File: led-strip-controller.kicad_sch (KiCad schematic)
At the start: 20 parts, among them J1 5.5/2.1, J2 PROG, J3 LED strip, Q1 BD681, Q2 BD681, Q3 BD681, SW1 PRG, SW2 RST, U1 12V->3V3, U2 ESP-201

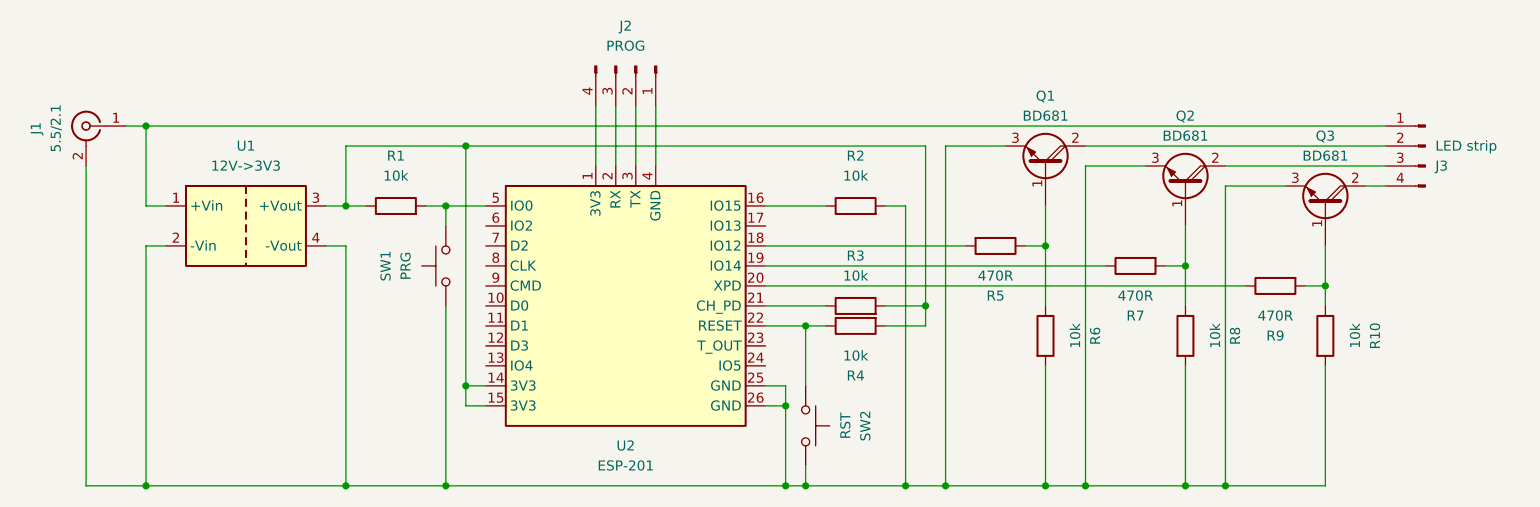
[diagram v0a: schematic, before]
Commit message: PINs 12, 13 and 14 used instead of 12, 14 and 16 (the original configuration caused flashing while device restarting)
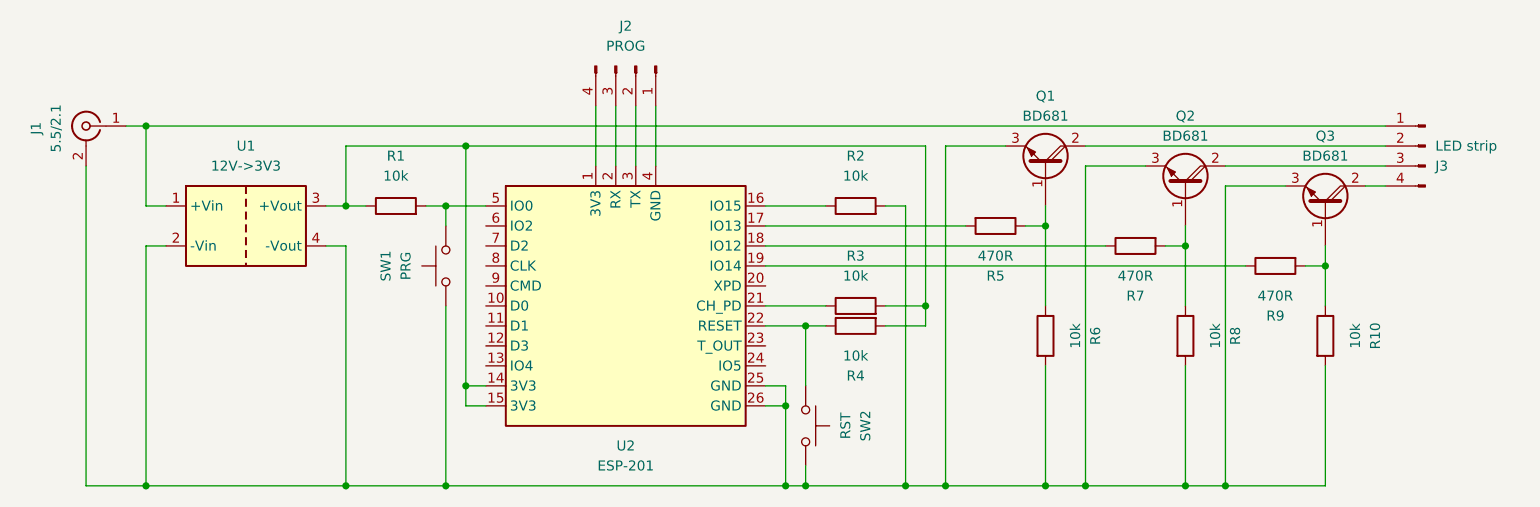
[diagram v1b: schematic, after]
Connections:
- net at U2.17 (IO13): now also R5.2
- net at U2.18 (IO12): now also R7.1; no longer R5.2
- net at U2.19 (IO14): now also R9.1; no longer R7.1
- net at U2.20 (XPD): no longer R9.1
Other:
- moved on the sheet: R5, R7, R9
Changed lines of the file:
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@@
 		(title "LED strip controller")
 		(date "2024-09-21")
-		(rev "1.0")
+		(rev "1.1")
 		(company "Eli Nucknack")
 	)
@@
 	)
 	(junction
-		(at 190.5 88.9)
-		(diameter 0)
-		(color 0 0 0 0)
-	)
-	(junction
 		(at 114.3 119.38)
 		(diameter 0)
@@
 	)
 	(junction
-		(at 208.28 91.44)
-		(diameter 0)
-		(color 0 0 0 0)
-	)
-	(junction
 		(at 175.26 96.52)
 		(diameter 0)
@@
 	)
 	(junction
+		(at 208.28 88.9)
+		(diameter 0)
+		(color 0 0 0 0)
+	)
+	(junction
 		(at 116.84 76.2)
 		(diameter 0)
@@
 	)
 	(junction
-		(at 226.06 93.98)
+		(at 226.06 91.44)
 		(diameter 0)
 		(color 0 0 0 0)
@@
 	)
 	(junction
+		(at 190.5 86.36)
+		(diameter 0)
+		(color 0 0 0 0)
+	)
+	(junction
 		(at 190.5 119.38)
 		(diameter 0)
@@
 	(wire
 		(pts
-			(xy 208.28 91.44) (xy 208.28 96.52)
-		)
-		(stroke
-			(width 0)
-			(type default)
-		)
-	)
-	(wire
-		(pts
 			(xy 172.72 119.38) (xy 177.8 119.38)
 		)
@@
 	(wire
 		(pts
-			(xy 154.94 88.9) (xy 180.34 88.9)
-		)
-		(stroke
-			(width 0)
-			(type default)
-		)
-	)
-	(wire
-		(pts
 			(xy 116.84 76.2) (xy 116.84 106.68)
 		)
@@
 	(wire
 		(pts
-			(xy 190.5 83.82) (xy 190.5 88.9)
+			(xy 190.5 83.82) (xy 190.5 86.36)
 		)
 		(stroke
@@
 	(wire
 		(pts
-			(xy 226.06 93.98) (xy 226.06 96.52)
+			(xy 226.06 91.44) (xy 226.06 96.52)
 		)
 		(stroke
@@
 	(wire
 		(pts
-			(xy 187.96 88.9) (xy 190.5 88.9)
+			(xy 187.96 86.36) (xy 190.5 86.36)
+		)
+		(stroke
+			(width 0)
+			(type default)
+		)
+	)
+	(wire
+		(pts
+			(xy 154.94 91.44) (xy 215.9 91.44)
 		)
 		(stroke
@@
 	(wire
 		(pts
-			(xy 223.52 93.98) (xy 226.06 93.98)
+			(xy 223.52 91.44) (xy 226.06 91.44)
 		)
 		(stroke
@@
 	(wire
 		(pts
-			(xy 154.94 93.98) (xy 215.9 93.98)
-		)
-		(stroke
-			(width 0)
-			(type default)
-		)
-	)
-	(wire
-		(pts
 			(xy 172.72 83.82) (xy 170.18 83.82)
 		)
@@
 	(wire
 		(pts
-			(xy 154.94 91.44) (xy 198.12 91.44)
-		)
-		(stroke
-			(width 0)
-			(type default)
-		)
-	)
-	(wire
-		(pts
 			(xy 135.89 71.12) (xy 135.89 78.74)
 		)
@@
 	(wire
 		(pts
-			(xy 226.06 88.9) (xy 226.06 93.98)
+			(xy 208.28 88.9) (xy 208.28 96.52)
+		)
+		(stroke
+			(width 0)
+			(type default)
+		)
+	)
+	(wire
+		(pts
+			(xy 226.06 88.9) (xy 226.06 91.44)
 		)
 		(stroke
@@
 	(wire
 		(pts
+			(xy 154.94 86.36) (xy 180.34 86.36)
+		)
+		(stroke
+			(width 0)
+			(type default)
+		)
+	)
+	(wire
+		(pts
 			(xy 76.2 119.38) (xy 101.6 119.38)
 		)
@@
 	(wire
 		(pts
+			(xy 190.5 86.36) (xy 190.5 96.52)
+		)
+		(stroke
+			(width 0)
+			(type default)
+		)
+	)
+	(wire
+		(pts
 			(xy 154.94 99.06) (xy 160.02 99.06)
 		)
@@
 	(wire
 		(pts
-			(xy 208.28 86.36) (xy 208.28 91.44)
+			(xy 208.28 86.36) (xy 208.28 88.9)
+		)
+		(stroke
+			(width 0)
+			(type default)
+		)
+	)
+	(wire
+		(pts
+			(xy 154.94 88.9) (xy 198.12 88.9)
 		)
 		(stroke
@@
 	(wire
 		(pts
-			(xy 190.5 88.9) (xy 190.5 96.52)
-		)
-		(stroke
-			(width 0)
-			(type default)
-		)
-	)
-	(wire
-		(pts
 			(xy 104.14 83.82) (xy 101.6 83.82)
 		)
@@
 	(wire
 		(pts
-			(xy 205.74 91.44) (xy 208.28 91.44)
+			(xy 205.74 88.9) (xy 208.28 88.9)
 		)
 		(stroke
@@
 	(symbol
 		(lib_id "Device:R")
-		(at 219.71 93.98 90)
+		(at 219.71 91.44 90)
 		(mirror x)
 		(unit 1)
@@
 		(dnp no)
 		(property "Reference" "R9"
-			(at 219.71 100.33 90)
+			(at 219.71 97.79 90)
 			(effects
 				(font
@@
 		)
 		(property "Value" "470R"
-			(at 219.71 97.79 90)
+			(at 219.71 95.25 90)
 			(effects
 				(font
@@
 		)
 		(property "Footprint" ""
-			(at 219.71 92.202 90)
+			(at 219.71 89.662 90)
 			(effects
 				(font
@@
 		)
 		(property "Datasheet" "~"
-			(at 219.71 93.98 0)
+			(at 219.71 91.44 0)
 			(effects
 				(font
@@
 		)
 		(property "Description" "Resistor"
-			(at 219.71 93.98 0)
+			(at 219.71 91.44 0)
 			(effects
 				(font
@@
 	(symbol
 		(lib_id "Device:R")
-		(at 201.93 91.44 90)
+		(at 201.93 88.9 90)
 		(mirror x)
 		(unit 1)
@@
 		(dnp no)
 		(property "Reference" "R7"
-			(at 201.93 97.79 90)
+			(at 201.93 95.25 90)
 			(effects
 				(font
@@
 		)
 		(property "Value" "470R"
-			(at 201.93 95.25 90)
+			(at 201.93 92.71 90)
 			(effects
 				(font
@@
 		)
 		(property "Footprint" ""
-			(at 201.93 89.662 90)
+			(at 201.93 87.122 90)
 			(effects
 				(font
@@
 		)
 		(property "Datasheet" "~"
-			(at 201.93 91.44 0)
+			(at 201.93 88.9 0)
 			(effects
 				(font
@@
 		)
 		(property "Description" "Resistor"
-			(at 201.93 91.44 0)
+			(at 201.93 88.9 0)
 			(effects
 				(font
@@
 	(symbol
 		(lib_id "Device:R")
-		(at 184.15 88.9 270)
+		(at 184.15 86.36 270)
 		(unit 1)
 		(exclude_from_sim no)
@@
 		(dnp no)
 		(property "Reference" "R5"
-			(at 184.15 95.25 90)
+			(at 184.15 92.71 90)
 			(effects
 				(font
@@
 		)
 		(property "Value" "470R"
-			(at 184.15 92.71 90)
+			(at 184.15 90.17 90)
 			(effects
 				(font
@@
 		)
 		(property "Footprint" ""
-			(at 184.15 87.122 90)
+			(at 184.15 84.582 90)
 			(effects
 				(font
@@
 		)
 		(property "Datasheet" "~"
-			(at 184.15 88.9 0)
+			(at 184.15 86.36 0)
 			(effects
 				(font
@@
 		)
 		(property "Description" "Resistor"
-			(at 184.15 88.9 0)
-			(effects
-				(font
+			(at 184.15 86.36 0)
+			(effects
+				(font

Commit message: The detachable DC-DC converter replaced with LM1085IT-3.3, internal antenne used for ESP-201
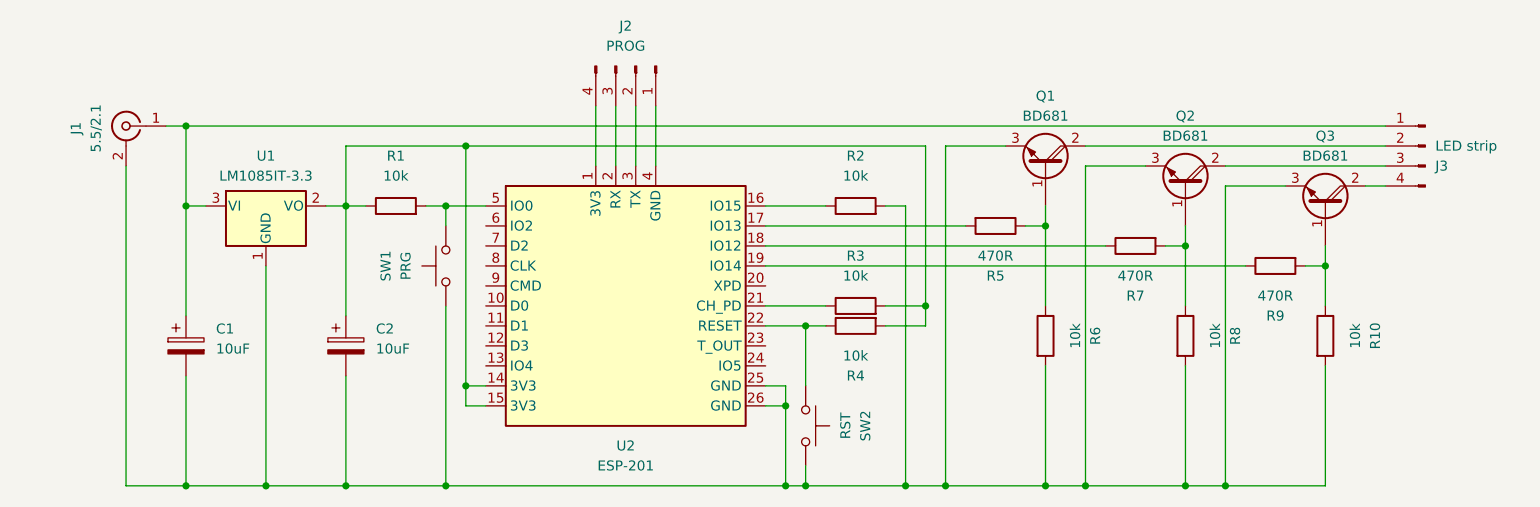
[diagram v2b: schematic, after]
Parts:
- removed U1: 12V->3V3, symbol led-strip-controller:DC-DC_converter
- added C1, C2: 10uF, symbol Device:C_Polarized
- added U1: LM1085IT-3.3, symbol Regulator_Linear:LM1085-3.3
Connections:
- net at J1.2 (Ext), Q1.3 (E), Q2.3 (E)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: now also C1.2, C2.2, U1.1 (GND)
- net at R1.1, R3.2, R4.2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: now also C2.1, U1.2 (VO)
- net at J1.1 (In), J3.1 (Pin_1): now also C1.1, U1.3 (VI)
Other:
- moved on the sheet: J1

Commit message: MQTT topics split to topics for the device state and topics for control, PCB documentation added, the case 3D model added, documentation adjusted
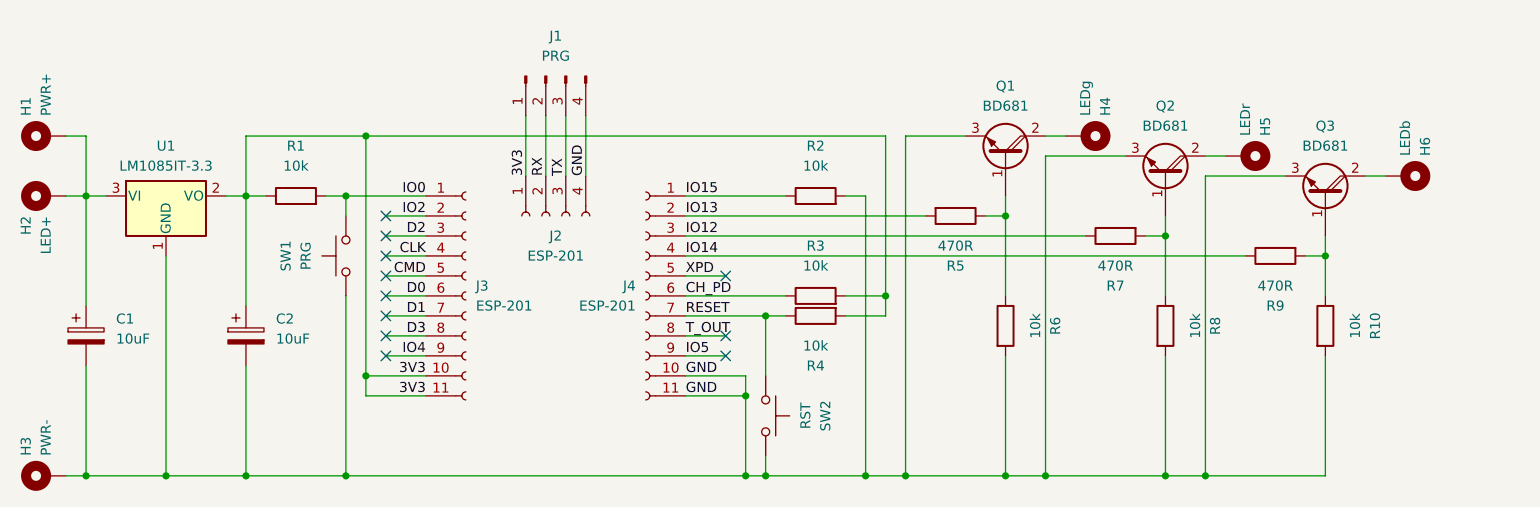
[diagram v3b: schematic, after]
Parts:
- removed J1: 5.5/2.1, symbol Connector:Conn_Coaxial
- removed J3: LED strip, symbol Connector:Conn_01x04_Pin
- removed U2: ESP-201, symbol led-strip-controller:ESP-201
- added H1: PWR+, symbol Mechanical:MountingHole_Pad
- added H2: LED+, symbol Mechanical:MountingHole_Pad
- added H3: PWR-, symbol Mechanical:MountingHole_Pad
- added H4: LEDg, symbol Mechanical:MountingHole_Pad
- added H5: LEDr, symbol Mechanical:MountingHole_Pad
- added H6: LEDb, symbol Mechanical:MountingHole_Pad
- added J2: ESP-201, symbol Connector:Conn_01x04_Socket
- added J3, J4: ESP-201, symbol Connector:Conn_01x11_Socket
- J1: renamed from J2; value PROG -> PRG
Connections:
- net GND: now reaches C1.2, C2.2, Q1.3 (E), Q2.3 (E), Q3.3 (E), R10.2, R2.2, R6.2, R8.2, SW1.2, SW2.2, U1.1 (GND)
- net GND: now also J1.4 (Pin_4), H3.1, J2.4 (Pin_4), J4.10 (Pin_10), J4.11 (Pin_11)
- net RESET: now reaches R4.1, SW2.1
- net RESET: now also J4.7 (Pin_7)
- net 3V3: now reaches C2.1, R1.1, R3.2, R4.2, U1.2 (VO)
- net 3V3: now also J1.1 (Pin_1), J2.1 (Pin_1), J3.10 (Pin_10), J3.11 (Pin_11)
- net IO0: now reaches R1.2, SW1.1
- net IO0: now also J3.1 (Pin_1)
- net CH_PD: now reaches R3.1
- net CH_PD: now also J4.6 (Pin_6)
- net RX: now reaches J1.2 (Pin_2)
- net RX: now also J2.2 (Pin_2)
- net TX: now reaches J1.3 (Pin_3)
- net TX: now also J2.3 (Pin_3)
- net IO15: now reaches R2.1
- net IO15: now also J4.1 (Pin_1)
- net IO13: now reaches R5.2
- net IO13: now also J4.2 (Pin_2)
- net IO12: now reaches R7.1
- net IO12: now also J4.3 (Pin_3)
- net IO14: now reaches R9.1
- net IO14: now also J4.4 (Pin_4)
- net at Q1.2 (C): now also H4.1
- net at C1.1, U1.3 (VI): now also H1.1, H2.1
- net at Q2.2 (C): now also H5.1
- net at Q3.2 (C): now also H6.1
- new net CLK: J3.4 (Pin_4)
- new net CMD: J3.5 (Pin_5)
- new net D0: J3.6 (Pin_6)
- new net D1: J3.7 (Pin_7)
- new net D2: J3.3 (Pin_3)
- new net D3: J3.8 (Pin_8)
- new net IO2: J3.2 (Pin_2)
- new net IO4: J3.9 (Pin_9)
- new net IO5: J4.9 (Pin_9)
- new net T_OUT: J4.8 (Pin_8)
- new net XPD: J4.5 (Pin_5)
- no-connect marks 0 -> 11
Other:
- moved on the sheet: C1, C2, J1, Q1, Q2, Q3, R1, R10, R2, R3, R4, R5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
